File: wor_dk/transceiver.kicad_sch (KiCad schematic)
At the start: 25 parts, among them J301 SMA, U301 Si4467, Y301 26MHz

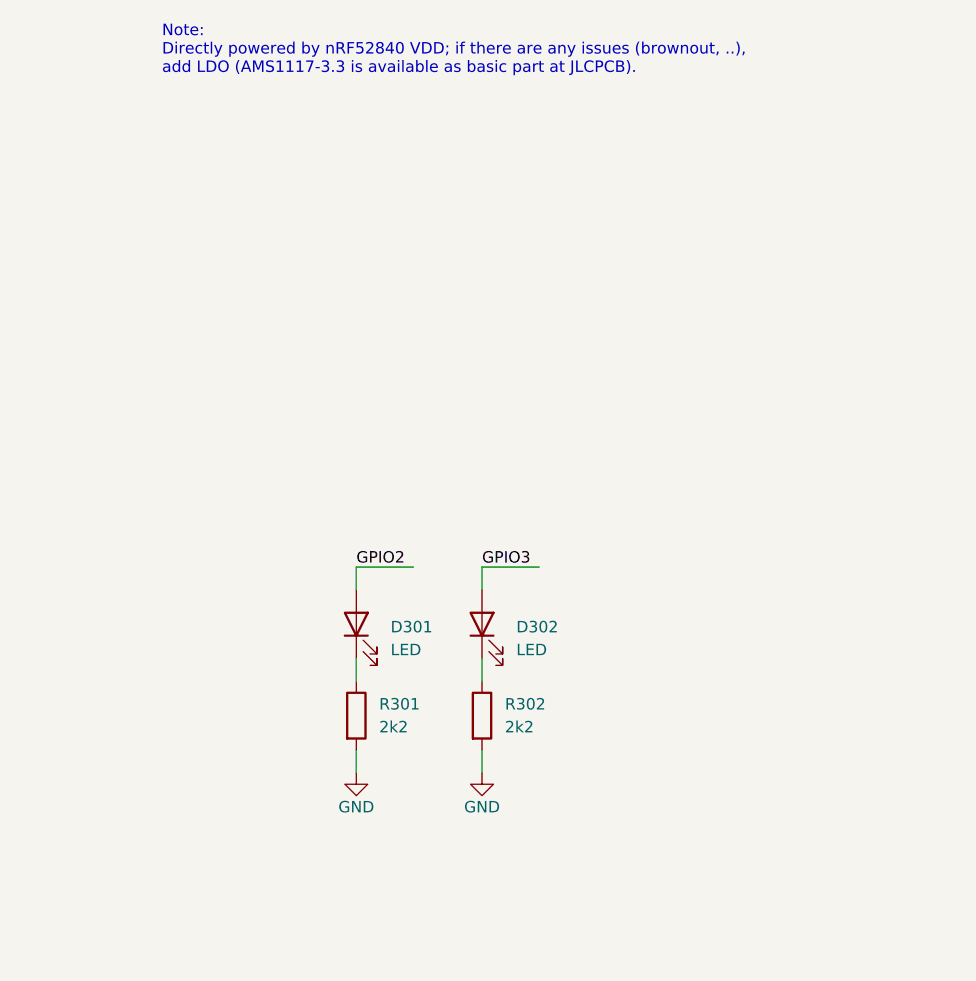
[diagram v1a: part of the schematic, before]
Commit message: wor_dk: high-level adjustments for main MCU, transceiver & controller
Main MCU:
- populate 32 kHz crystal (remove DNP)
- populate programming connector (remove DNP)
- remove power LED
- remove application LED
- remove user button
- remove Bluetooth parts
- remove USB connector & parts

Transceiver:
- remove RX/TX LEDs

Controller MCU:
- populate programming connector (remove DNP)
- remove 32 kHz crystal & capacitors
- remove Bluetooth parts
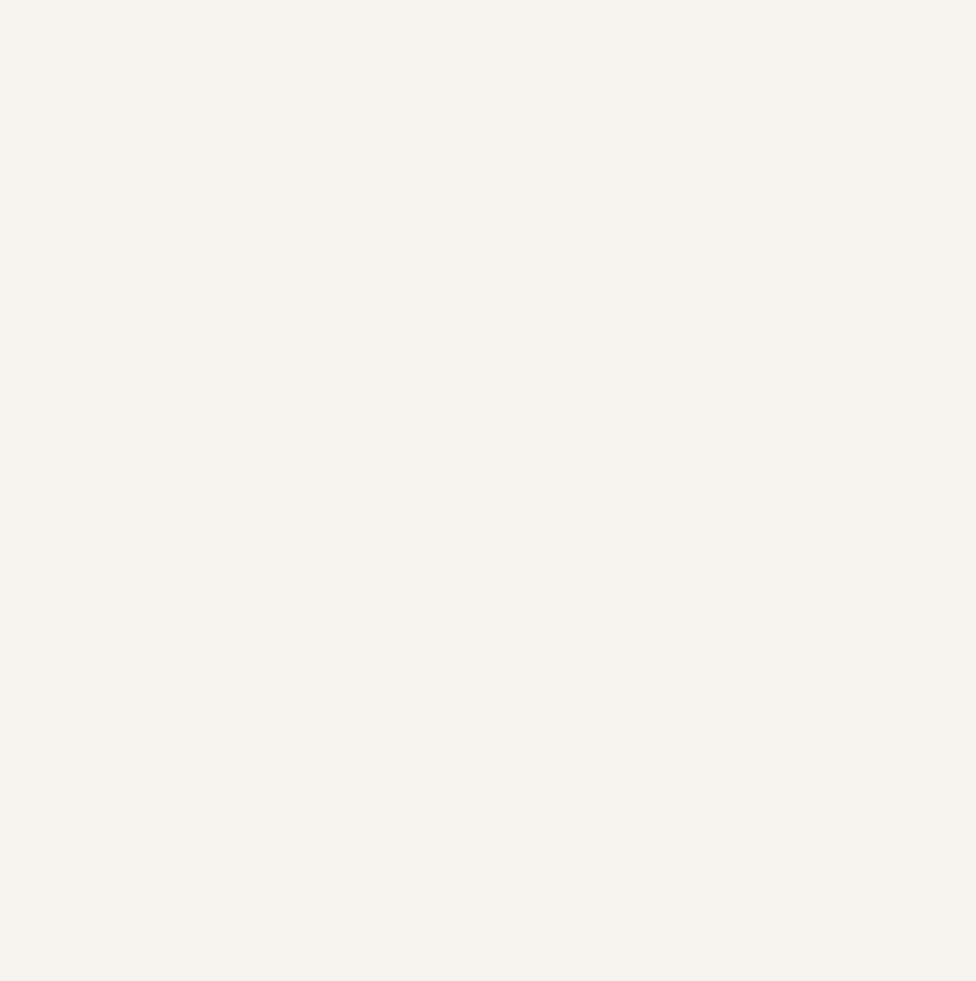
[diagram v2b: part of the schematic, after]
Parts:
- removed D301, D302: LED, LED_SMD:LED_0805_2012Metric, symbol Device:LED
- removed R301, R302: 2k2, Resistor_SMD:R_0402_1005Metric, symbol Device:R
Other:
- note removed: "Note: Directly powered by nRF52840 VDD; if there are any issues (brownout, ..), add LDO (AMS1117-3.3 is available as basic part at JLCPCB)."

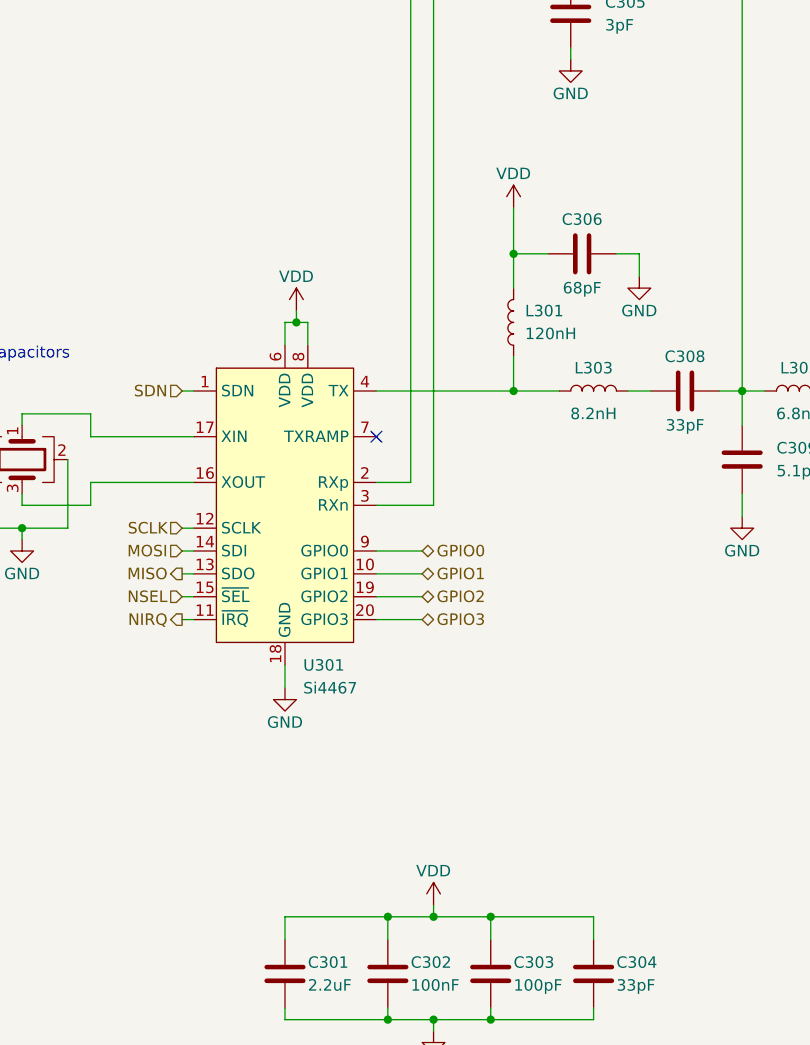
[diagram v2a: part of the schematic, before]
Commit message: wor_dk: adapt main MCU power supply to externally powered
The main MCU now has support for enabling DC/DC converter for REG1 as
per reference circuit configuration no. 5.
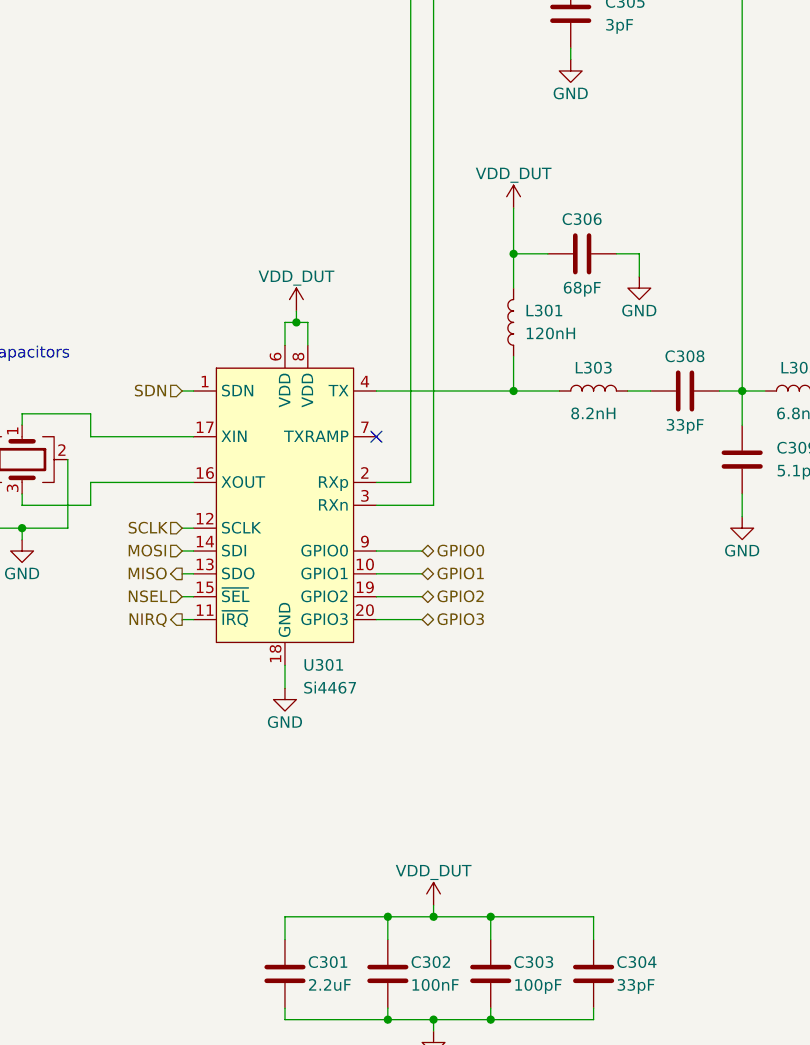
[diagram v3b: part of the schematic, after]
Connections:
- net VDD renamed VDD_DUT
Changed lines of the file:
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@@
 			)
 		)
-		(property "Value" "VDD"
+		(property "Value" "VDD_DUT"
 			(at 82.55 76.2 0)
 			(effects
@@
 			)
 		)
-		(property "Value" "VDD"
+		(property "Value" "VDD_DUT"
 			(at 106.68 64.77 0)
 			(effects
@@
 			)
 		)
-		(property "Value" "VDD"
+		(property "Value" "VDD_DUT"
 			(at 97.79 142.24 0)
 			(effects

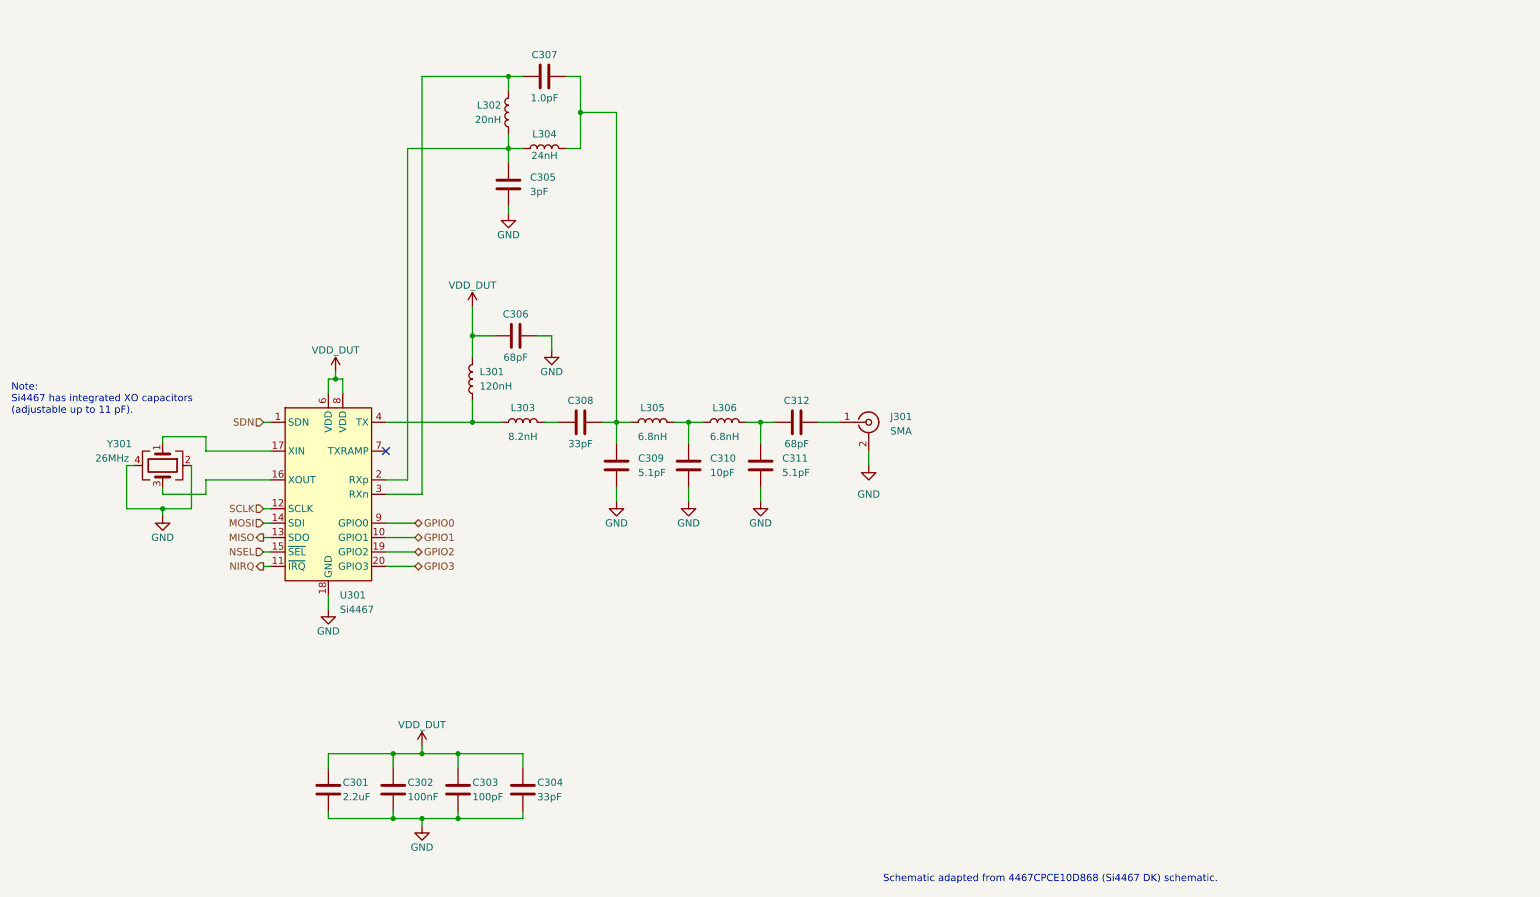
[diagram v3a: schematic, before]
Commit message: wor_dk: remove controller & re-annotate schematics
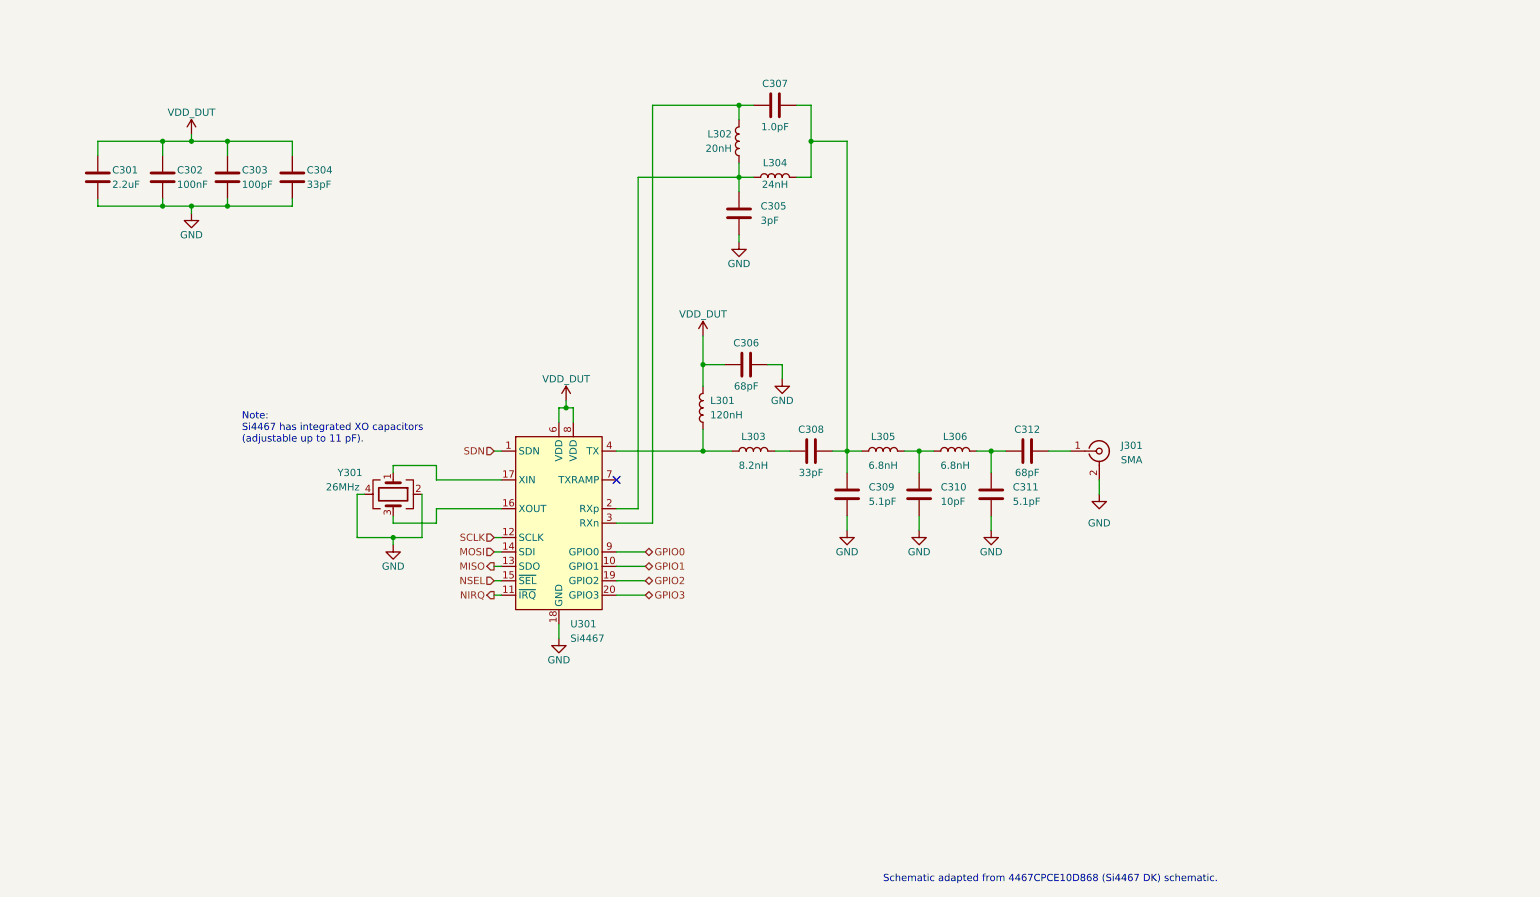
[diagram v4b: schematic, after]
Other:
- moved on the sheet: C301, C302, C303, C304, C305, C306, C307, C308, C309, C310, C311, C312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

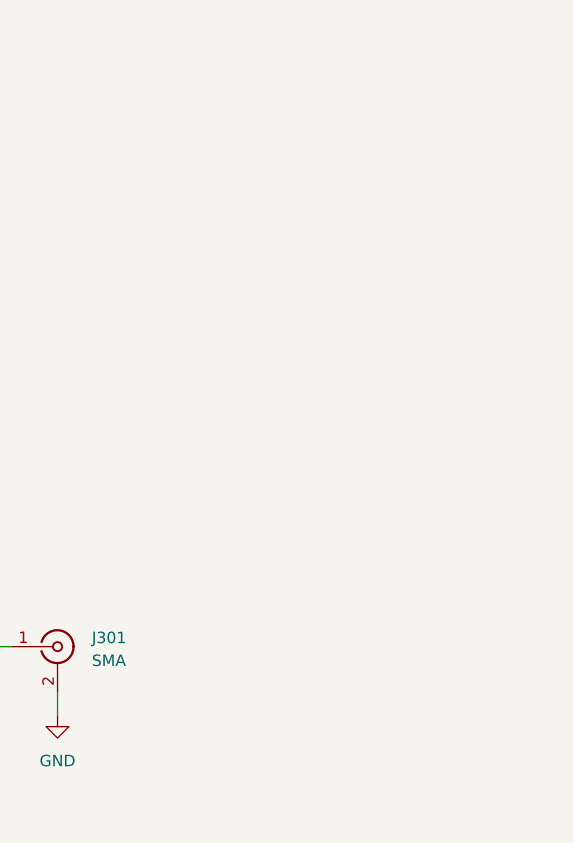
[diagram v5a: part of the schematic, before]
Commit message: wor_dk: add not populated pin-headers for Si4467 signals
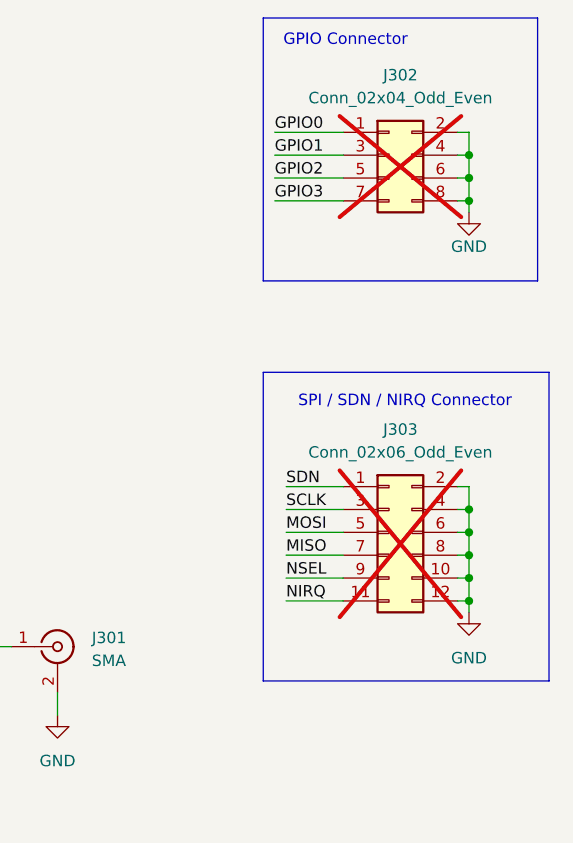
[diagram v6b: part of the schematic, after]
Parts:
- added J302: Conn_02x04_Odd_Even, Connector_PinHeader_2.54mm:PinHeader_2x04_P2.54mm_Vertical, symbol Connector_Generic:Conn_02x04_Odd_Even
- added J303: Conn_02x06_Odd_Even, Connector_PinHeader_2.54mm:PinHeader_2x06_P2.54mm_Vertical, symbol Connector_Generic:Conn_02x06_Odd_Even
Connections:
- net GND: now also J302.2 (Pin_2), J302.4 (Pin_4), J302.6 (Pin_6), J302.8 (Pin_8), J303.10 (Pin_10), J303.12 (Pin_12), J303.2 (Pin_2), J303.4 (Pin_4), J303.6 (Pin_6), J303.8 (Pin_8)
- net GPIO0: now also J302.1 (Pin_1)
- net GPIO1: now also J302.3 (Pin_3)
- net GPIO2: now also J302.5 (Pin_5)
- net GPIO3: now also J302.7 (Pin_7)
- net MISO: now also J303.7 (Pin_7)
- net MOSI: now also J303.5 (Pin_5)
- net NIRQ: now also J303.11 (Pin_11)
- net NSEL: now also J303.9 (Pin_9)
- net SCLK: now also J303.3 (Pin_3)
- net SDN: now also J303.1 (Pin_1)
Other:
- note added: "GPIO Connector"
- note added: "SPI / SDN / NIRQ Connector"

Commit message: wor_dk: add footprints & part info for all capacitors
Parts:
- C301: MPN (none) -> CL05A225MQ5NSNC
- C302: MPN (none) -> GRM033R61E104KE14D
- C303: MPN (none) -> GRM0335C1H101JA01D
- C304, C308: MPN (none) -> CC0201JRNPO8BN330
- C305: MPN (none) -> GJM0335C1E3R0CB01D
- C306, C312: MPN (none) -> GRM0335C1H680GA01D
- C307: MPN (none) -> GJM0335C1H1R0BB01D
- C309, C311: MPN (none) -> GRM0335C1H5R1BA01D
- C310: MPN (none) -> GJM0335C1E100GB01D
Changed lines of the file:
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@@
+			)
+		)
+		(property "MPN" "GJM0335C1E100GB01D"
+			(at 185.42 101.6 0)
+			(effects
+				(font
+					(size 1.27 1.27)
+				)
+				(hide yes)
 			)
 		)
@@
 			)
 		)
-		(property "Datasheet" "~"
+		(property "Datasheet" "https://wmsc.lcsc.com/wmsc/upload/file/pdf/v2/lcsc/2304140030_Samsung-Electro-Mechanics-CL05A225MQ5NSNC_C12530.pdf"
 			(at 40.64 45.72 0)
 			(effects
@@
 		)
 		(property "Part Number" "CL05A225MQ5NSNC"
+			(at 40.64 45.72 0)
+			(effects
+				(font
+					(size 1.27 1.27)
+				)
+				(hide yes)
+			)
+		)
+		(property "MPN" "CL05A225MQ5NSNC"
 			(at 40.64 45.72 0)
 			(effects
@@
 		)
 		(property "Part Number" "GJM0335C1H1R0BB01D"
+			(at 160.02 33.02 0)
+			(effects
+				(font
+					(size 1.27 1.27)
+				)
+				(hide yes)
+			)
+		)
+		(property "MPN" "GJM0335C1H1R0BB01D"
 			(at 160.02 33.02 0)
 			(effects
@@
 			)
 		)
+		(property "MPN" "GJM0335C1E3R0CB01D"
+			(at 153.67 52.07 0)
+			(effects
+				(font
+					(size 1.27 1.27)
+				)
+				(hide yes)
+			)
+		)
 		(pin "1"
 		)
@@
 			)
 		)
-		(property "Datasheet" "~"
+		(property "Datasheet" "https://wmsc.lcsc.com/wmsc/upload/file/pdf/v2/lcsc/2004231433_YAGEO-CC0201JRNPO8BN330_C513616.pdf"
 			(at 74.93 45.72 0)
 			(effects
@@
 		)
 		(property "Part Number" "CC0201JRNPO8BN330"
+			(at 74.93 45.72 0)
+			(effects
+				(font
+					(size 1.27 1.27)
+				)
+				(hide yes)
+			)
+		)
+		(property "MPN" "CC0201JRNPO8BN330"
 			(at 74.93 45.72 0)
 			(effects
@@
 			)
 		)
-		(property "Datasheet" "~"
+		(property "Datasheet" "https://wmsc.lcsc.com/wmsc/upload/file/pdf/v2/lcsc/2004231433_YAGEO-CC0201JRNPO8BN330_C513616.pdf"
 			(at 166.37 93.98 0)
 			(effects
@@
 		)
 		(property "Part Number" "CC0201JRNPO8BN330"
+			(at 166.37 93.98 0)
+			(effects
+				(font
+					(size 1.27 1.27)
+				)
+				(hide yes)
+			)
+		)
+		(property "MPN" "CC0201JRNPO8BN330"
 			(at 166.37 93.98 0)
 			(effects
@@
 			)
 		)
-		(property "Datasheet" "~"
+		(property "Datasheet" "https://wmsc.lcsc.com/wmsc/upload/file/pdf/v2/lcsc/2304140030_Murata-Electronics-GRM0335C1H5R1BA01D_C441749.pdf"
 			(at 172.72 101.6 0)
 			(effects
@@
 		)
 		(property "Part Number" "GRM0335C1H5R1BA01D"
+			(at 172.72 101.6 0)
+			(effects
+				(font
+					(size 1.27 1.27)
+				)
+				(hide yes)
+			)
+		)
+		(property "MPN" "GRM0335C1H5R1BA01D"
 			(at 172.72 101.6 0)
 			(effects
@@
 			)
 		)
-		(property "Datasheet" "~"
+		(property "Datasheet" "https://wmsc.lcsc.com/wmsc/upload/file/pdf/v2/lcsc/2304140030_Murata-Electronics-GRM0335C1H5R1BA01D_C441749.pdf"
 			(at 198.12 101.6 0)
 			(effects
@@
 		)
 		(property "Part Number" "GRM0335C1H5R1BA01D"
+			(at 198.12 101.6 0)
+			(effects
+				(font
+					(size 1.27 1.27)
+				)
+				(hide yes)
+			)
+		)
+		(property "MPN" "GRM0335C1H5R1BA01D"
 			(at 198.12 101.6 0)
 			(effects
@@
 			)
 		)
-		(property "Datasheet" "~"
+		(property "Datasheet" "https://wmsc.lcsc.com/wmsc/upload/file/pdf/v2/lcsc/2304140030_Murata-Electronics-GRM0335C1H680GA01D_C161433.pdf"
 			(at 154.94 78.74 0)
 			(effects
@@
 		)
 		(property "Part Number" "GRM0335C1H680GA01D"
+			(at 154.94 78.74 0)
+			(effects
+				(font
+					(size 1.27 1.27)
+				)
+				(hide yes)
+			)
+		)
+		(property "MPN" "GRM0335C1H680GA01D"
 			(at 154.94 78.74 0)
 			(effects
@@
 			)
 		)
-		(property "Datasheet" "~"
+		(property "Datasheet" "https://wmsc.lcsc.com/wmsc/upload/file/pdf/v2/lcsc/1811081531_Murata-Electronics-GRM0335C1H101JA01D_C76922.pdf"
 			(at 63.5 45.72 0)
 			(effects
@@
 		)
 		(property "Part Number" "GRM0335C1H101JA01D"
+			(at 63.5 45.72 0)
+			(effects
+				(font
+					(size 1.27 1.27)
+				)
+				(hide yes)
+			)
+		)
+		(property "MPN" "GRM0335C1H101JA01D"
 			(at 63.5 45.72 0)
 			(effects
@@
 			)
 		)
-		(property "Datasheet" "~"
+		(property "Datasheet" "https://wmsc.lcsc.com/wmsc/upload/file/pdf/v2/lcsc/2304140030_Murata-Electronics-GRM0335C1H680GA01D_C161433.pdf"
 			(at 204.47 93.98 0)
 			(effects
@@
 		)
 		(property "Part Number" "GRM0335C1H680GA01D"
+			(at 204.47 93.98 0)
+			(effects
+				(font
+					(size 1.27 1.27)
+				)
+				(hide yes)
+			)
+		)
+		(property "MPN" "GRM0335C1H680GA01D"
 			(at 204.47 93.98 0)
 			(effects
@@
 			)
 		)
-		(property "Datasheet" "~"
+		(property "Datasheet" "https://wmsc.lcsc.com/wmsc/upload/file/pdf/v2/lcsc/1811081532_Murata-Electronics-GRM033R61E104KE14D_C76939.pdf"
 			(at 52.07 45.72 0)
 			(effects
@@
 			(at 52.07 45.72 0)
 			(effects
+				(font
+					(size 1.27 1.27)
+				)
+				(hide yes)
+			)
+		)
+		(property "MPN" "GRM033R61E104KE14D"
+			(at 52.07 45.72 0)
+			(effects
